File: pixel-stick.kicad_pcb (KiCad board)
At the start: 2 copper layers, 16.5 x 37.1 mm, 15 parts, among them J2 WS28**, U1 AZ1117-3.3, U2 ESP-01v090, U3 SN74LVC1T45DBV, U4 RT9361A

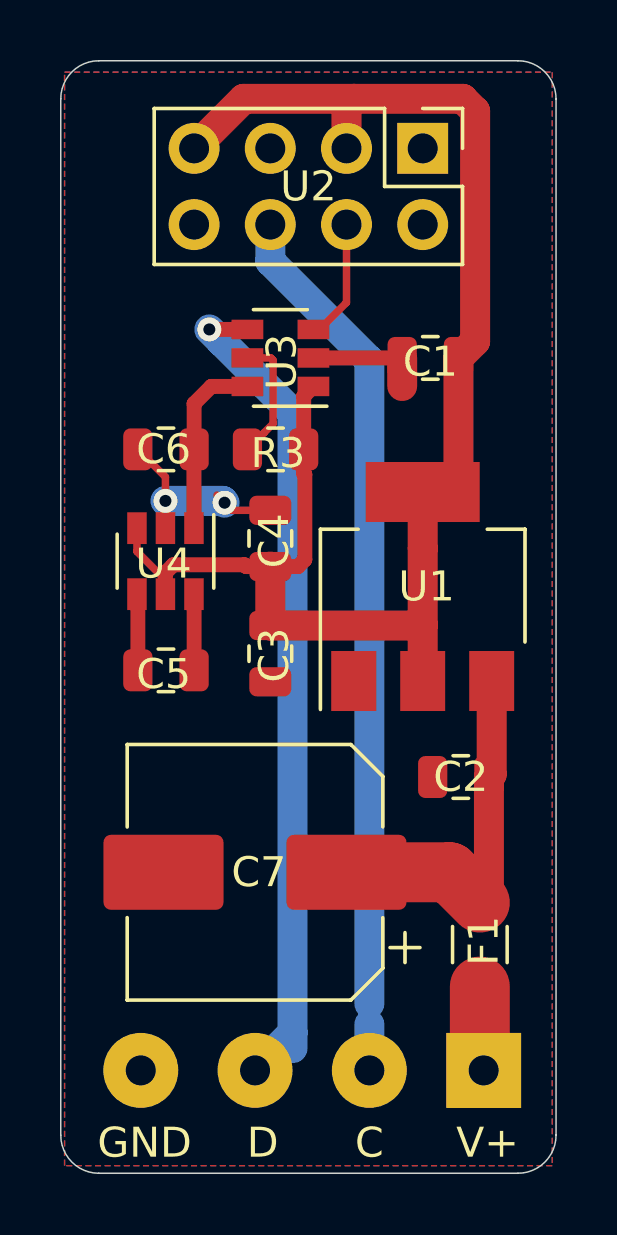
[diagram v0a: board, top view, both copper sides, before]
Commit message: use fills for power
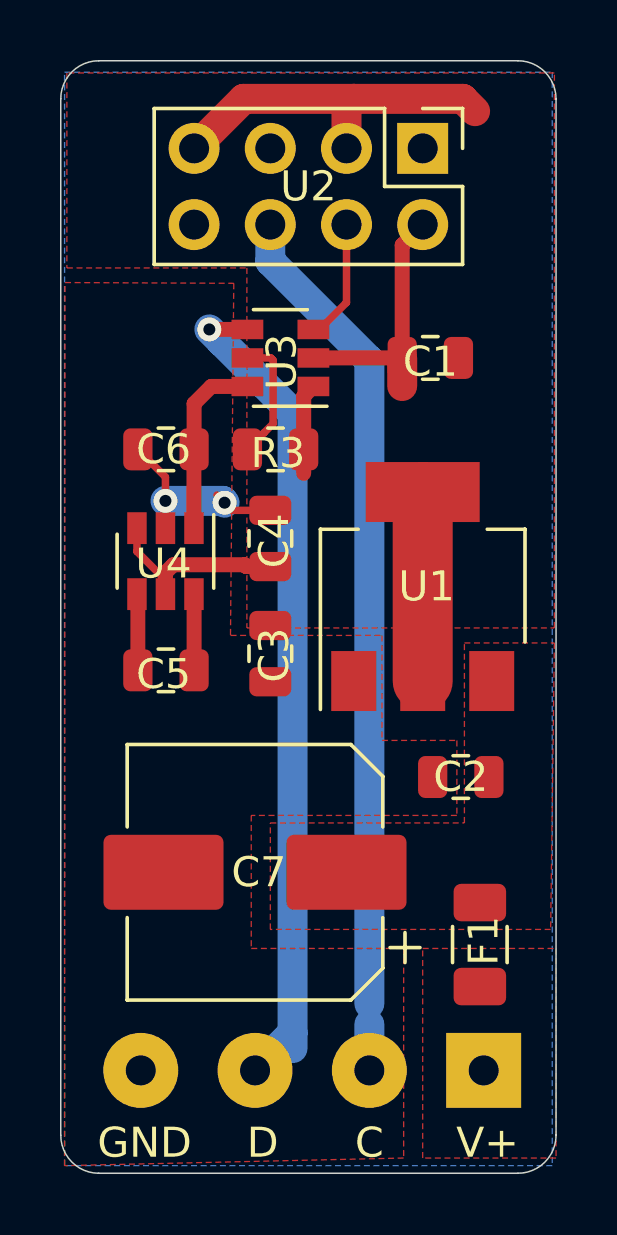
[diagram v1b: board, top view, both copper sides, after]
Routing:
- net +3V3: track 52.5 -> 28.3 mm
- net +VDC: track 12.4 -> 0.00 mm
- net GND: track 13.3 -> 18.1 mm
- net /VIN: track 3.22 -> 0.05 mm
- added copper zone on F.Cu, net +3V3
- added copper zone on F.Cu, net +VDC
- added copper zone on F.Cu, net /VIN
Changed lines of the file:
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@@
     (thickness 1.6)
     (drawings 13)
-    (tracks 82)
+    (tracks 64)
     (zones 0)
     (modules 15)
@@
   )
   (setup
-    (last_trace_width 1)
+    (last_trace_width 2)
     (user_trace_width 0.5)
     (user_trace_width 1)
@@
   (segment (start 46.035 68.265) (end 47.945 68.265) (width 1) (layer B.Cu) (net 1))
   (segment (start 53.9265 63.5) (end 50.968 63.5) (width 0.5) (layer F.Cu) (net 1))
-  (segment (start 49.53 70.455) (end 49.53 72.42) (width 1) (layer F.Cu) (net 2))
-  (segment (start 54.58 72.42) (end 54.61 72.39) (width 1) (layer F.Cu) (net 2))
-  (segment (start 54.61 72.39) (end 54.61 74.27) (width 1) (layer F.Cu) (net 2))
-  (segment (start 49.53 72.42) (end 54.58 72.42) (width 1) (layer F.Cu) (net 2))
-  (segment (start 54.61 67.97) (end 54.61 69.85) (width 1) (layer F.Cu) (net 2))
+  (segment (start 53.9265 59.7385) (end 54.61 59.055) (width 0.5) (layer F.Cu) (net 1))
+  (segment (start 53.9265 63.5) (end 53.9265 59.7385) (width 0.5) (layer F.Cu) (net 1))
   (segment (start 45.085 69.954) (end 46.035 70.904) (width 0.25) (layer F.Cu) (net 2))
   (segment (start 46.035 70.904) (end 46.035 71.374) (width 0.25) (layer F.Cu) (net 2))
@@
   (segment (start 46.299999 70.393999) (end 48.668999 70.393999) (width 0.5) (layer F.Cu) (net 2))
   (segment (start 46.035 71.374) (end 46.035 70.658998) (width 0.5) (layer F.Cu) (net 2))
-  (segment (start 50.643 67.348) (end 50.68001 67.38501) (width 0.5) (layer F.Cu) (net 2))
-  (segment (start 50.68001 67.38501) (end 50.68001 70.22399) (width 0.5) (layer F.Cu) (net 2))
   (segment (start 50.643 66.548) (end 50.643 67.348) (width 0.5) (layer F.Cu) (net 2))
-  (segment (start 50.449 70.455) (end 49.53 70.455) (width 0.5) (layer F.Cu) (net 2))
-  (segment (start 50.68001 70.22399) (end 50.449 70.455) (width 0.5) (layer F.Cu) (net 2))
   (segment (start 50.643 64.775) (end 50.968 64.45) (width 0.5) (layer F.Cu) (net 2))
   (segment (start 50.643 66.548) (end 50.643 64.775) (width 0.5) (layer F.Cu) (net 2))
-  (segment (start 54.61 69.85) (end 54.61 72.39) (width 1) (layer F.Cu) (net 2))
   (segment (start 46.99 56.515) (end 48.641 54.864) (width 1) (layer F.Cu) (net 2))
   (segment (start 52.07 56.515) (end 52.07 55.118) (width 1) (layer F.Cu) (net 2))
   (segment (start 52.07 55.118) (end 52.324 54.864) (width 1) (layer F.Cu) (net 2))
   (segment (start 48.641 54.864) (end 52.324 54.864) (width 1) (layer F.Cu) (net 2))
-  (segment (start 56.357737 62.943763) (end 55.8015 63.5) (width 1) (layer F.Cu) (net 2))
-  (segment (start 56.357737 55.275535) (end 56.357737 62.943763) (width 1) (layer F.Cu) (net 2))
   (segment (start 55.946202 54.864) (end 56.357737 55.275535) (width 1) (layer F.Cu) (net 2))
   (segment (start 52.324 54.864) (end 55.946202 54.864) (width 1) (layer F.Cu) (net 2))
-  (segment (start 55.8015 63.5) (end 55.8015 68.072) (width 1) (layer F.Cu) (net 2))
   (segment (start 52.04 56.485) (end 52.07 56.515) (width 0.25) (layer B.Cu) (net 2))
-  (segment (start 56.515 81.655) (end 55.505 80.645) (width 2) (layer F.Cu) (net 3))
-  (segment (start 55.505 80.645) (end 52.07 80.645) (width 2) (layer F.Cu) (net 3))
-  (segment (start 56.91 77.3775) (end 56.8175 77.47) (width 1) (layer F.Cu) (net 3))
-  (segment (start 56.91 74.27) (end 56.91 77.3775) (width 1) (layer F.Cu) (net 3))
-  (segment (start 56.8175 81.3525) (end 56.515 81.655) (width 1) (layer F.Cu) (net 3))
-  (segment (start 56.8175 77.47) (end 56.8175 81.3525) (width 1) (layer F.Cu) (net 3))
+  (segment (start 54.61 74.27) (end 54.61 67.97) (width 2) (layer F.Cu) (net 2))
   (segment (start 45.115 71.404) (end 45.085 71.374) (width 0.5) (layer F.Cu) (net 4))
   (segment (start 45.115 73.914) (end 45.115 71.404) (width 0.5) (layer F.Cu) (net 4))
@@
   (segment (start 46.985 66.553) (end 46.99 66.548) (width 0.5) (layer F.Cu) (net 6))
   (segment (start 46.985 69.174) (end 46.985 66.553) (width 0.5) (layer F.Cu) (net 6))
-  (segment (start 56.515 84.455) (end 56.515 86.36) (width 2) (layer F.Cu) (net 8))
   (segment (start 56.525836 87.132837) (end 56.510734 87.158438) (width 1) (layer F.Cu) (net 8))
   (segment (start 56.515 87.122) (end 56.525836 87.132837) (width 1) (layer F.Cu) (net 8))
-  (segment (start 56.515 85.852) (end 56.515 87.122) (width 1) (layer F.Cu) (net 8))
   (segment (start 52.832 87.249) (end 52.832 85.717) (width 1) (layer B.Cu) (net 10))
   (segment (start 47.498 62.55) (end 48.768 62.55) (width 0.5) (layer F.Cu) (net 11))
@@
     (polygon
       (pts
-        (xy 42.672 53.975) (xy 58.928 53.975) (xy 58.928 90.424) (xy 42.672 90.424)
+        (xy 42.687563 60.9875) (xy 48.312438 61.0125) (xy 48.203125 72.75) (xy 53.25 72.75) (xy 53.25 76.25)
+        (xy 55.75 76.25) (xy 55.75 78.75) (xy 48.895 78.75) (xy 48.895 83.185) (xy 53.975 83.185)
+        (xy 53.975 90.17) (xy 42.672 90.424)
       )
     )
@@
       )
     )
+  )
+  (zone (net 3) (net_name +VDC) (layer F.Cu) (hatch edge 0.508)
+    (connect_pads (clearance 0.508))
+    (min_thickness 0.254)
+    (fill yes (arc_segments 32) (thermal_gap 0.508) (thermal_bridge_width 0.508))
+    (polygon
+      (pts
+        (xy 56 73) (xy 59 73) (xy 58.875 82.55) (xy 49.53 82.55) (xy 49.53 79)
+        (xy 56 79)
+      )
+    )
+  )
+  (zone (net 2) (net_name +3V3) (layer F.Cu) (hatch edge 0.508)
+    (connect_pads (clearance 0.508))
+    (min_thickness 0.254)
+    (fill yes (arc_segments 32) (thermal_gap 0.508) (thermal_bridge_width 0.508))
+    (polygon
+      (pts
+        (xy 48.75 72.5) (xy 53.75 72.5) (xy 59 72.5) (xy 59 54) (xy 42.75 54)
+        (xy 42.75 60.5) (xy 48.75 60.5)
+      )
+    )
+  )
+  (zone (net 8) (net_name /VIN) (layer F.Cu) (hatch edge 0.508)
+    (connect_pads (clearance 0.508))
+    (min_thickness 0.254)
+    (fill yes (arc_segments 32) (thermal_gap 0.508) (thermal_bridge_width 0.508))
+    (polygon
+      (pts
+        (xy 54.61 83.185) (xy 59.055 83.185) (xy 59.055 90.17) (xy 54.61 90.17)
+      )
+    )

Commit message: cleanup flooded planes
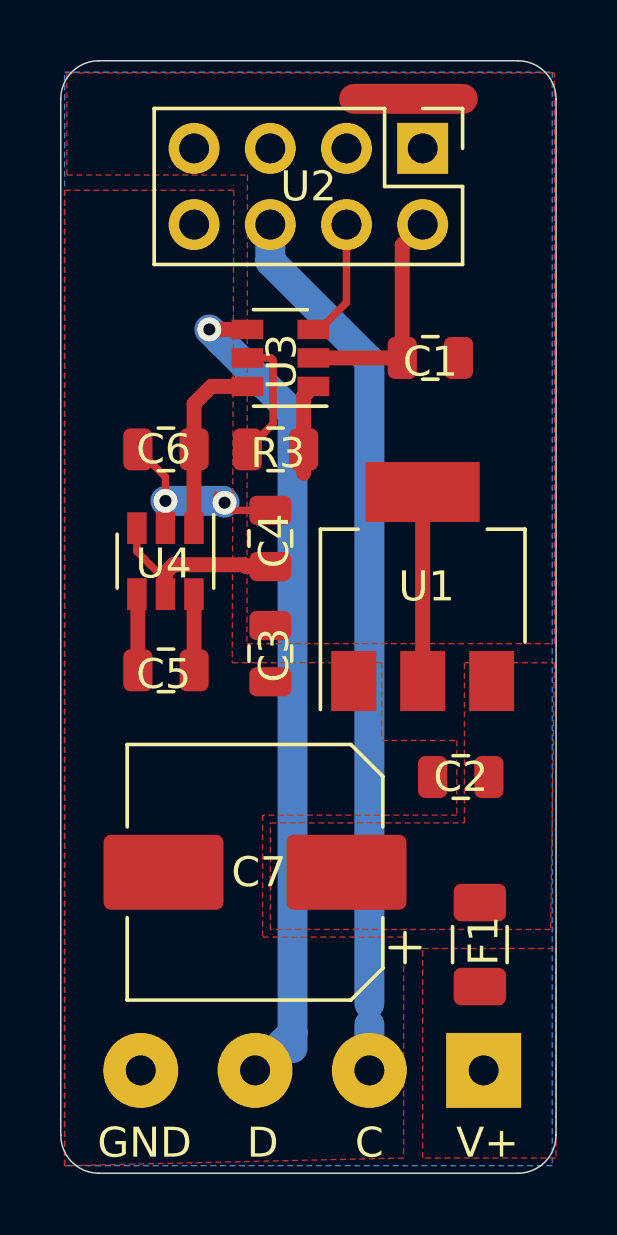
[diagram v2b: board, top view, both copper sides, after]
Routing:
- net +3V3: track 28.3 -> 19.9 mm
- net GND: track 18.1 -> 17.1 mm
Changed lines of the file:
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@@
     (thickness 1.6)
     (drawings 13)
-    (tracks 64)
+    (tracks 57)
     (zones 0)
     (modules 15)
@@
       (outputformat 1)
       (mirror false)
-      (drillshape 1)
+      (drillshape 0)
       (scaleselection 1)
-      (outputdirectory ""))
+      (outputdirectory "gerbers"))
   )
   (net 0 "")
@@
   (segment (start 46.035 68.265) (end 46.035 69.174) (width 0.25) (layer F.Cu) (net 1))
   (via (at 46.035 68.265) (size 0.8) (drill 0.4) (layers F.Cu B.Cu) (net 1))
-  (segment (start 53.9265 63.5) (end 53.9265 64.4375) (width 1) (layer F.Cu) (net 1))
-  (segment (start 53.9265 64.4375) (end 53.9265 64.4375) (width 1) (layer F.Cu) (net 1))
   (segment (start 47.945 68.265) (end 48.006 68.326) (width 1) (layer B.Cu) (net 1))
   (segment (start 46.035 68.265) (end 47.945 68.265) (width 1) (layer B.Cu) (net 1))
@@
   (segment (start 50.643 64.775) (end 50.968 64.45) (width 0.5) (layer F.Cu) (net 2))
   (segment (start 50.643 66.548) (end 50.643 64.775) (width 0.5) (layer F.Cu) (net 2))
-  (segment (start 46.99 56.515) (end 48.641 54.864) (width 1) (layer F.Cu) (net 2))
-  (segment (start 52.07 56.515) (end 52.07 55.118) (width 1) (layer F.Cu) (net 2))
-  (segment (start 52.07 55.118) (end 52.324 54.864) (width 1) (layer F.Cu) (net 2))
-  (segment (start 48.641 54.864) (end 52.324 54.864) (width 1) (layer F.Cu) (net 2))
-  (segment (start 55.946202 54.864) (end 56.357737 55.275535) (width 1) (layer F.Cu) (net 2))
   (segment (start 52.324 54.864) (end 55.946202 54.864) (width 1) (layer F.Cu) (net 2))
   (segment (start 52.04 56.485) (end 52.07 56.515) (width 0.25) (layer B.Cu) (net 2))
-  (segment (start 54.61 74.27) (end 54.61 67.97) (width 2) (layer F.Cu) (net 2))
+  (segment (start 54.61 74.27) (end 54.61 67.97) (width 0.5) (layer F.Cu) (net 2))
   (segment (start 45.115 71.404) (end 45.085 71.374) (width 0.5) (layer F.Cu) (net 4))
   (segment (start 45.115 73.914) (end 45.115 71.404) (width 0.5) (layer F.Cu) (net 4))
@@
     (polygon
       (pts
-        (xy 42.687563 60.9875) (xy 48.312438 61.0125) (xy 48.203125 72.75) (xy 53.25 72.75) (xy 53.25 76.25)
-        (xy 55.75 76.25) (xy 55.75 78.75) (xy 48.895 78.75) (xy 48.895 83.185) (xy 53.975 83.185)
+        (xy 42.672 57.912) (xy 48.312438 57.912) (xy 48.26 73.66) (xy 53.25 73.66) (xy 53.25 76.25)
+        (xy 55.75 76.25) (xy 55.75 78.74) (xy 49.276 78.74) (xy 49.276 82.804) (xy 53.975 82.804)
         (xy 53.975 90.17) (xy 42.672 90.424)
       )
@@
     (polygon
       (pts
-        (xy 56 73) (xy 59 73) (xy 58.875 82.55) (xy 49.53 82.55) (xy 49.53 79)
+        (xy 56 73.66) (xy 59 73.66) (xy 58.875 82.55) (xy 49.53 82.55) (xy 49.53 79)
         (xy 56 79)
       )
@@
     (polygon
       (pts
-        (xy 48.75 72.5) (xy 53.75 72.5) (xy 59 72.5) (xy 59 54) (xy 42.75 54)
-        (xy 42.75 60.5) (xy 48.75 60.5)
+        (xy 48.75 73.025) (xy 59 73.025) (xy 59 54) (xy 42.75 54) (xy 42.75 57.404)
+        (xy 48.768 57.404)
       )
     )

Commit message: improve decoupling cap placement for ESP
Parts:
- moved C1 12.2 mm to (44.2, 57.7), turned to 270 degrees
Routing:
- net GND: track 17.1 -> 13.5 mm
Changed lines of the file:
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@@
     (thickness 1.6)
     (drawings 13)
-    (tracks 57)
+    (tracks 56)
     (zones 0)
     (modules 15)
@@
   )
   (setup
-    (last_trace_width 2)
+    (last_trace_width 0.5)
     (user_trace_width 0.5)
     (user_trace_width 1)
@@
   )
   (module Capacitor_SMD:C_0805_2012Metric (layer F.Cu)
-    (at 54.864 63.5 180)
+    (at 44.196 57.658 270)
     (descr "Capacitor SMD 0805 (2012 Metric), square (rectangular) end terminal, IPC_7351 nominal, (Body size source: https://docs.google.com/spreadsheets/d/1BsfQQcO9C6DZCsRaXUlFlo91Tg2WpOkGARC1WS5S8t0/edit?usp=sharing), generated with kicad-footprint-generator")
     (tags capacitor)
     (attr smd)
-    (fp_text reference C1 (at 0 -0.127) (layer F.SilkS)
-      (effects (font (size 1 1) (thickness 0.15)))
-    )
-    (fp_text value 10µF (at 0 1.65) (layer F.Fab)
-      (effects (font (size 1 1) (thickness 0.15)))
-    )
-    (fp_text user %R (at 0 0) (layer F.Fab)
+    (fp_text reference C1 (at 0 -0.127 90) (layer F.SilkS)
+      (effects (font (size 1 1) (thickness 0.15)))
+    )
+    (fp_text value 10µF (at 0 1.65 90) (layer F.Fab)
+      (effects (font (size 1 1) (thickness 0.15)))
+    )
+    (fp_text user %R (at 0 0 90) (layer F.Fab)
       (effects (font (size 0.5 0.5) (thickness 0.08)))
     )
@@
     (fp_line (start -1 -0.6) (end 1 -0.6) (layer F.Fab) (width 0.1))
     (fp_line (start -1 0.6) (end -1 -0.6) (layer F.Fab) (width 0.1))
-    (pad 2 smd roundrect (at 0.9375 0 180) (size 0.975 1.4) (layers F.Cu F.Paste F.Mask) (roundrect_rratio 0.25)
-      (net 1 GND))
-    (pad 1 smd roundrect (at -0.9375 0 180) (size 0.975 1.4) (layers F.Cu F.Paste F.Mask) (roundrect_rratio 0.25)
+    (pad 2 smd roundrect (at 0.9375 0 270) (size 0.975 1.4) (layers F.Cu F.Paste F.Mask) (roundrect_rratio 0.25)
+      (net 1 GND))
+    (pad 1 smd roundrect (at -0.9375 0 270) (size 0.975 1.4) (layers F.Cu F.Paste F.Mask) (roundrect_rratio 0.25)
       (net 2 +3V3))
     (model ${KISYS3DMOD}/Capacitor_SMD.3dshapes/C_0805_2012Metric.wrl
@@
   (gr_line (start 43.815 90.678) (end 57.785 90.678) (layer Edge.Cuts) (width 0.05))
   (gr_line (start 42.545 54.864) (end 42.545 89.408) (layer Edge.Cuts) (width 0.05))
-  (segment (start 53.4185 63.5) (end 50.968 63.5) (width 0.25) (layer F.Cu) (net 1))
   (segment (start 46.035 67.468) (end 46.035 68.265) (width 0.25) (layer F.Cu) (net 1))
   (segment (start 45.115 66.548) (end 46.035 67.468) (width 0.25) (layer F.Cu) (net 1))
@@
   (segment (start 47.945 68.265) (end 48.006 68.326) (width 1) (layer B.Cu) (net 1))
   (segment (start 46.035 68.265) (end 47.945 68.265) (width 1) (layer B.Cu) (net 1))
-  (segment (start 53.9265 63.5) (end 50.968 63.5) (width 0.5) (layer F.Cu) (net 1))
-  (segment (start 53.9265 59.7385) (end 54.61 59.055) (width 0.5) (layer F.Cu) (net 1))
-  (segment (start 53.9265 63.5) (end 53.9265 59.7385) (width 0.5) (layer F.Cu) (net 1))
+  (segment (start 51.998 63.5) (end 50.968 63.5) (width 0.5) (layer F.Cu) (net 1))
+  (segment (start 54.61 60.888) (end 51.998 63.5) (width 0.5) (layer F.Cu) (net 1))
+  (segment (start 54.61 59.055) (end 54.61 60.888) (width 0.5) (layer F.Cu) (net 1))
   (segment (start 45.085 69.954) (end 46.035 70.904) (width 0.25) (layer F.Cu) (net 2))
   (segment (start 46.035 70.904) (end 46.035 71.374) (width 0.25) (layer F.Cu) (net 2))
